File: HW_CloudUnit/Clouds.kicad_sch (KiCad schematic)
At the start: 28 parts, among them J1 Conn_01x06, J2 Conn_01x03, J3 Conn_01x04, J4 Conn_01x04, U1 STM32G030F6Px, U2 AS5600L-ASOM, U3 DRV8313PWPR

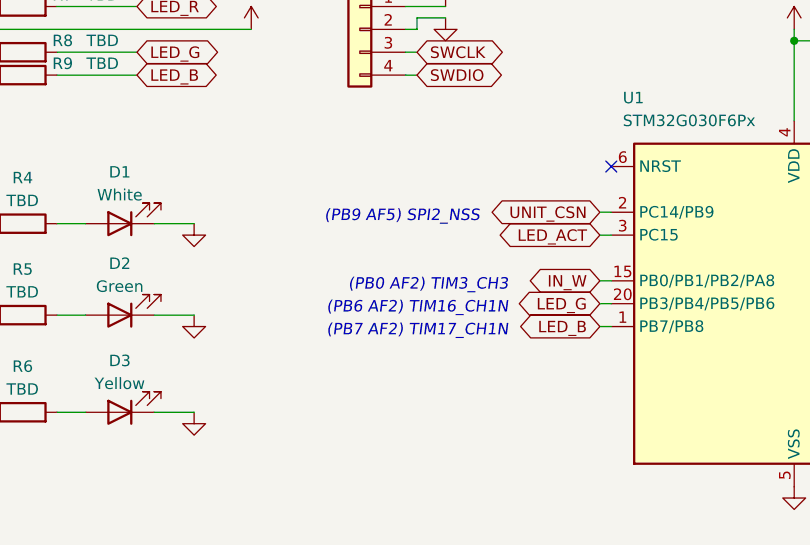
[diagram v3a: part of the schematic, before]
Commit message: (WIP) Output signals to the driver IC
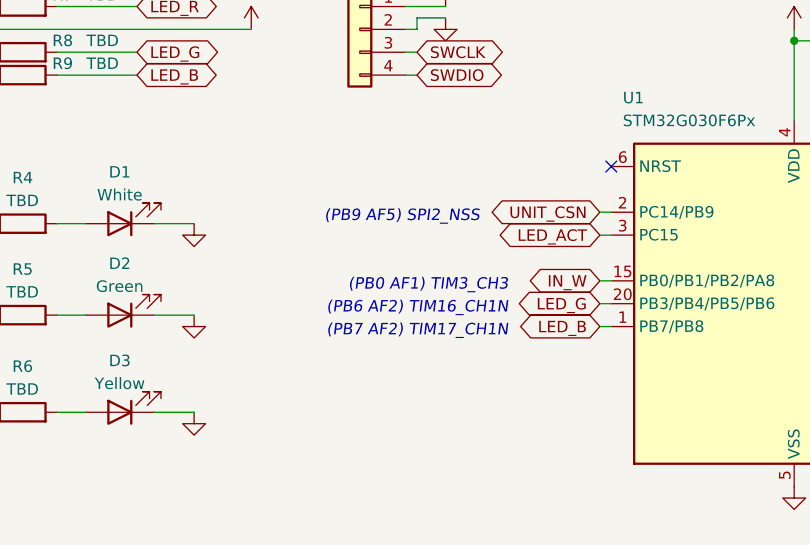
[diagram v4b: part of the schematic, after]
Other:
- note added: "(PB0 AF1) TIM3_CH3"
- note removed: "(PB0 AF2) TIM3_CH3"
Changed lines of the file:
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@@
     (effects (font (size 1.27 1.27) italic) (justify left bottom))
   )
-  (text "(PB0 AF2) TIM3_CH3" (at 92.71 104.14 0)
+  (text "(PB0 AF1) TIM3_CH3" (at 92.71 104.14 0)
     (effects (font (size 1.27 1.27) italic) (justify right bottom))
   )

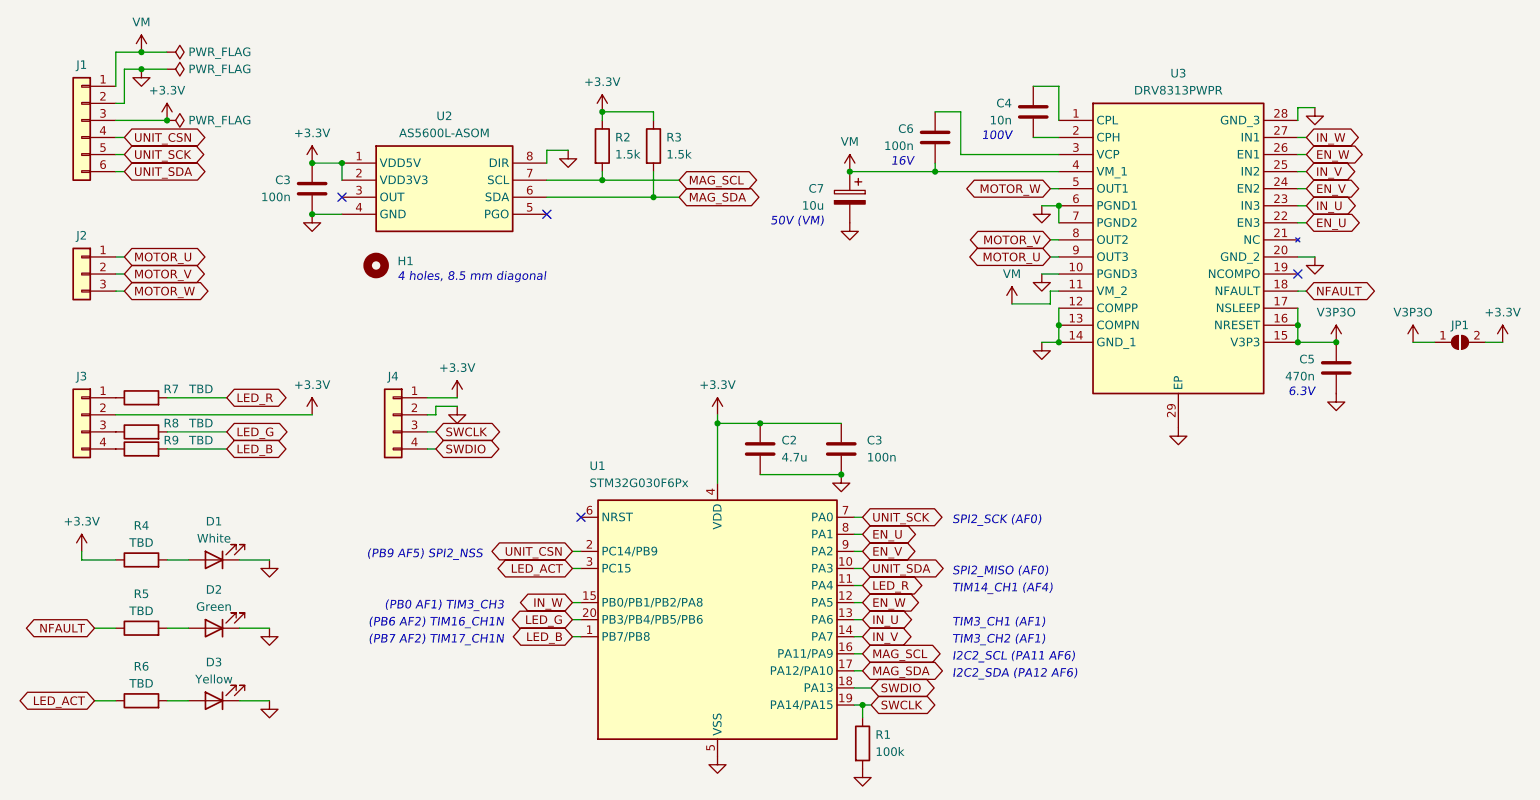
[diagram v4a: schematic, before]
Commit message: Update clouds unit PCB with new motor dimensions
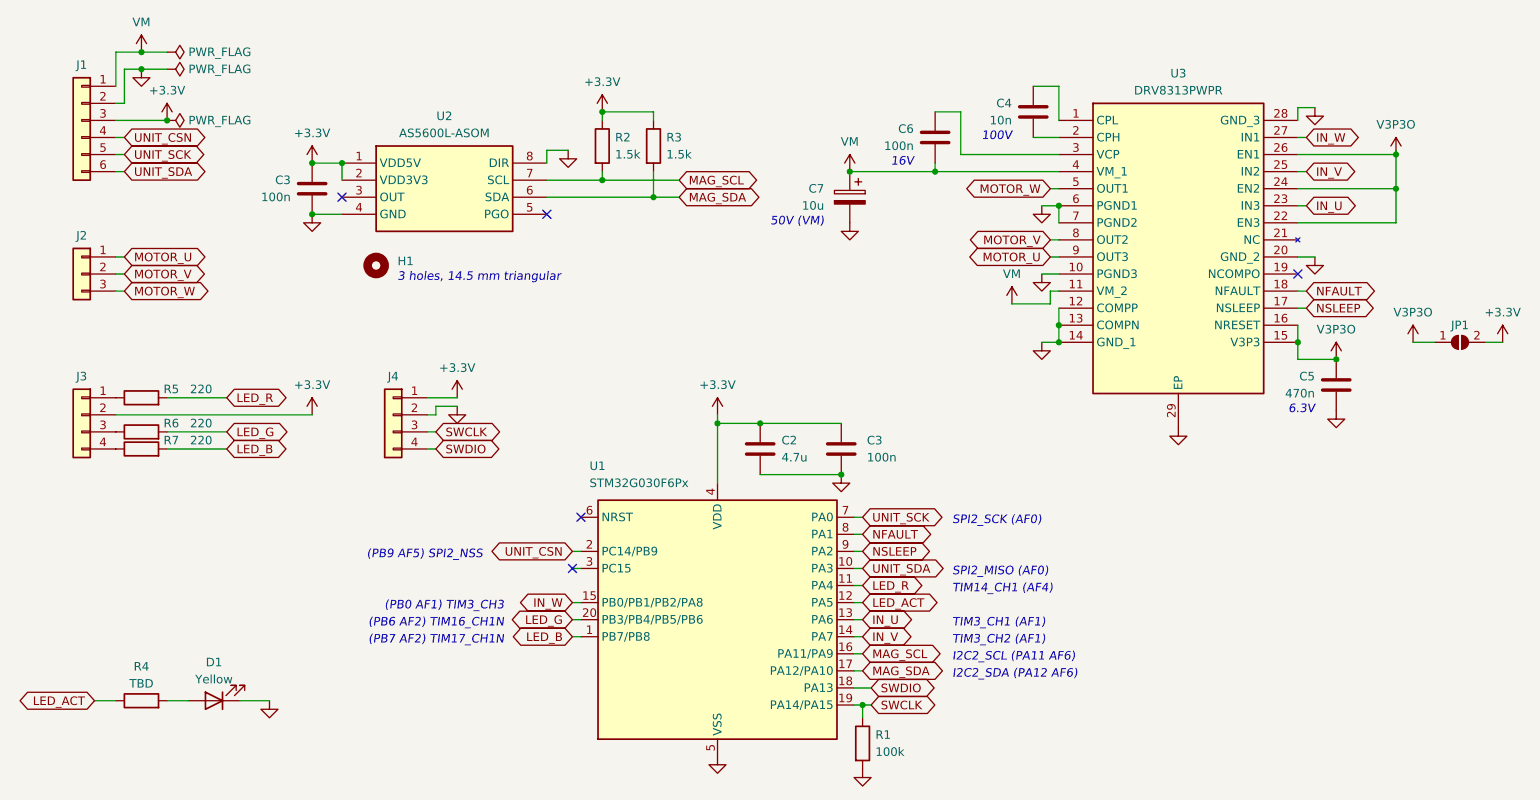
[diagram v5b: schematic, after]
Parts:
- removed D1: White, LED_SMD:LED_0603_1608Metric, symbol Device:LED
- removed D2: Green, LED_SMD:LED_0603_1608Metric, symbol Device:LED
- removed R4, R5: TBD, Resistor_SMD:R_0603_1608Metric, symbol Device:R
- C5: footprint Capacitor_SMD:C_0603_1608Metric -> Capacitor_SMD:C_0805_2012Metric
- H1: footprint Clouds_footprints:MountingHoles_M1.4_Diag8.5 -> Clouds_footprints:MountingHoles_M3_Tri14.5
- R5: renamed from R7; value TBD -> 220
- R6: renamed from R8; value TBD -> 220
- R7: renamed from R9; value TBD -> 220
- renumbered D3 to D1, R6 to R4
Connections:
- net LED_ACT: now also U1.12 (PA5); no longer U1.3 (PC15)
- net NFAULT: now also U1.8 (PA1)
- net V3P3O: now also U3.22 (EN3), U3.24 (EN2), U3.26 (EN1); no longer U3.17 (NSLEEP)
- removed net EN_U: U1.8 (PA1), U3.22 (EN3)
- net EN_V renamed NSLEEP
- net NSLEEP: now also U3.17 (NSLEEP); no longer U3.24 (EN2)
- removed net EN_W: U1.12 (PA5), U3.26 (EN1)
- no-connect marks 4 -> 5
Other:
- note added: "3 holes, 14.5 mm triangular"
- note removed: "4 holes, 8.5 mm diagonal"
- moved on the sheet: C5
